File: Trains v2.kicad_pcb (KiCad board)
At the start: 2 copper layers, 200 x 50 mm, 29 parts, among them Q1 2N3904, Q2 2N3904, Q3 2N3904, SW1 SW_SPST4, SW2 SW_SPST4

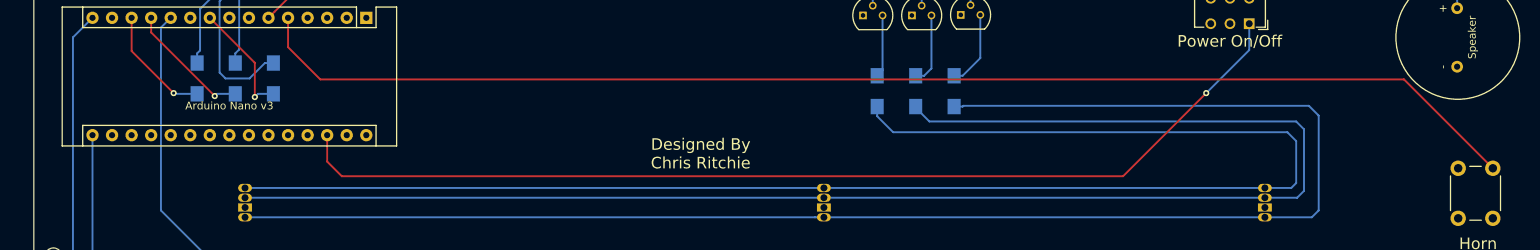
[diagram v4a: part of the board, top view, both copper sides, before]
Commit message: Add Acrylic Base
Add acrylic base
Add board #
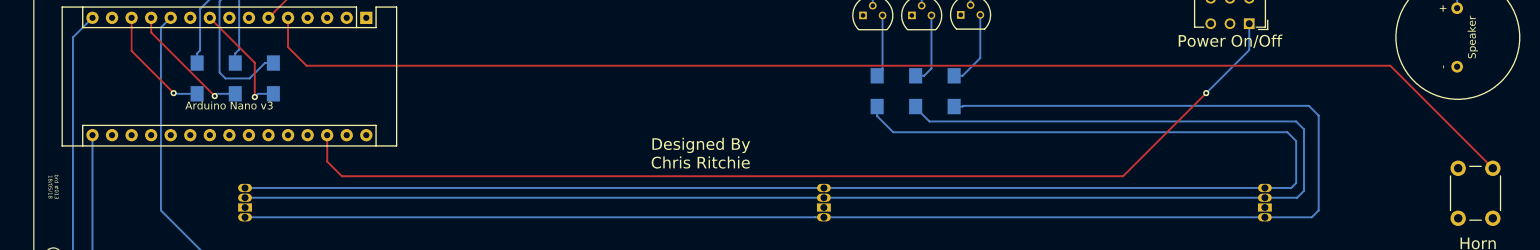
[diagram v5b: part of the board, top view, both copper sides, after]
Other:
- board text added: "brd #013 18/05/18"
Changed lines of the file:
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@@
-(kicad_pcb (version 20171130) (host pcbnew 5.0.0-rc2-dev-unknown-904eb82~65~ubuntu16.04.1)
+(kicad_pcb (version 20171130) (host pcbnew 5.0.0-rc2-dev-unknown-d09445c~65~ubuntu16.04.1)
   (general
     (thickness 1.6)
-    (drawings 15)
+    (drawings 16)
     (tracks 108)
     (zones 0)
@@
       (outputformat 1)
       (mirror false)
-      (drillshape 1)
+      (drillshape 0)
       (scaleselection 1)
-      (outputdirectory ""))
+      (outputdirectory GERBER/))
   )
   (net 0 "")
@@
       (xy 0.85912 -4.312342)) (layer F.Mask) (width 0.01))
   )
+  (gr_text "brd #013\n18/05/18" (at 2.54 30.099 270) (layer F.SilkS)
+    (effects (font (size 0.5 0.5) (thickness 0.125)))
+  )
   (gr_text "Add brd#" (at 8.128 60.325) (layer Eco1.User)
     (effects (font (size 1.5 2) (thickness 0.3)))
@@
   (segment (start 79.610001 1.796999) (end 36.811001 1.796999) (width 0.25) (layer F.Cu) (net 9))
   (segment (start 80.01 1.397) (end 79.610001 1.796999) (width 0.25) (layer F.Cu) (net 9))
-  (segment (start 189.5 27.668) (end 177.961 16.129) (width 0.25) (layer F.Cu) (net 10))
-  (segment (start 177.961 16.129) (end 37.211 16.129) (width 0.25) (layer F.Cu) (net 10))
-  (segment (start 37.211 16.129) (end 33.02 11.938) (width 0.25) (layer F.Cu) (net 10))
   (segment (start 33.02 11.938) (end 33.02 8.128) (width 0.25) (layer F.Cu) (net 10))
+  (segment (start 35.433 14.351) (end 33.02 11.938) (width 0.25) (layer F.Cu) (net 10))
+  (segment (start 176.183 14.351) (end 35.433 14.351) (width 0.25) (layer F.Cu) (net 10))
+  (segment (start 189.5 27.668) (end 176.183 14.351) (width 0.25) (layer F.Cu) (net 10))
   (segment (start 109.535 20.903) (end 111.619 22.987) (width 0.25) (layer B.Cu) (net 12))
   (segment (start 109.535 19.653) (end 109.535 20.903) (width 0.25) (layer B.Cu) (net 12))
